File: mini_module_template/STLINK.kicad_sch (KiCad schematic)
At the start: 25 parts, among them U6 STM32F103CB, Y2 8MHz

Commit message: Leyout rev 1
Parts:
- removed Y2: 8MHz, st-link:Crystal_SMD_5032-2Pin_5.0x3.2mm, symbol Device:Crystal
- added C27: 10u, Capacitor_SMD:C_0805_2012Metric, symbol Device:C
- added C37: 100nF, Capacitor_SMD:C_0402_1005Metric, symbol Device:C
- added FB2: FerriteBead, Inductor_SMD:L_0805_2012Metric, symbol Device:FerriteBead
- added Q1: S9013, Package_TO_SOT_SMD:SOT-23, symbol Device:Q_NPN_BEC
- added R18: 10k, Resistor_SMD:R_0402_1005Metric, symbol Device:R
- added R20: 100R, Resistor_SMD:R_0402_1005Metric, symbol Device:R
- added R21: 39k, Resistor_SMD:R_0402_1005Metric, symbol Device:R
- added R22: 1K5, Resistor_SMD:R_0402_1005Metric, symbol Device:R
- added Y2: 8MHz, Crystal:Crystal_SMD_3225-4Pin_3.2x2.5mm, symbol Device:Crystal_GND24
- R17: renamed from R34; footprint Resistor_SMD:R_0402_1005Metric -> Resistor_SMD:R_0603_1608Metric
- renumbered C26 to C13, C27 to C14, C28 to C15, C29 to C16, C21 to C17, C22 to C18, C23 to C19, D9 to D4, D10 to D5, R26 to R11, R27 to R12, R35 to R13, R29 to R14, R32 to R15, R36 to R16, R37 to R19, R38 to R23, U6 to U3
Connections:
- net +3V3: now also FB2.1, Q1.3 (C); no longer C13.1, C14.1, C15.1, C16.1, U3.1 (VBAT), U3.24 (VDD), U3.36 (VDD), U3.48 (VDD), U3.9 (VDDA)
- net BOOT: now also TP2.1; no longer TP4.1
- net CLK: now also TP4.1; no longer TP3.1
- net DIO: now also TP3.1; no longer TP2.1
- net GND: now also C27.2, C37.2, R21.1, Y2.2, Y2.4
- net USB_D+: now also R22.1
- net USB_RENUM: now also R20.1
- net at C19.1, U3.6 (PD1): now also Y2.3
- net at C18.1, U3.5 (PD0): now also Y2.1
- new net: C13.1, C14.1, C15.1, C16.1, C27.1, C37.1, FB2.2, U3.1 (VBAT), U3.24 (VDD), U3.36 (VDD), U3.48 (VDD), U3.9 (VDDA)
- new net: Q1.2 (E), R22.2
- new net: Q1.1 (B), R18.1, R20.2, R21.2
- new net +5V: R18.2
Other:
- note added: "FORCE RENUMERATION OF USB DEVICES"
- note added: "SWD"
- note removed: "Decoupling"
- note removed: "Programming Pins"
- moved on the sheet: C13, C14, C15, C16

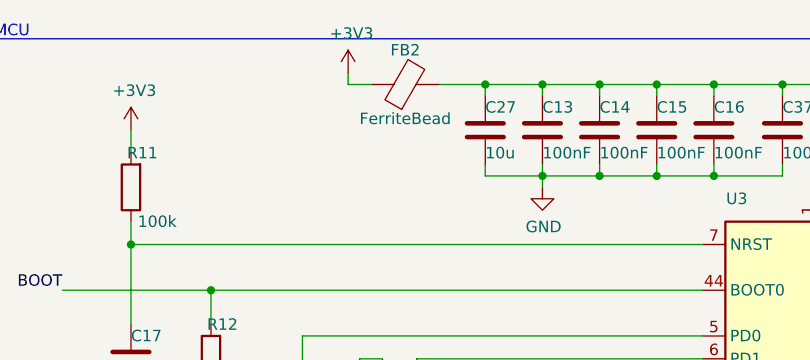
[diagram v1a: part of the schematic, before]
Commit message: fixed can and usb traces
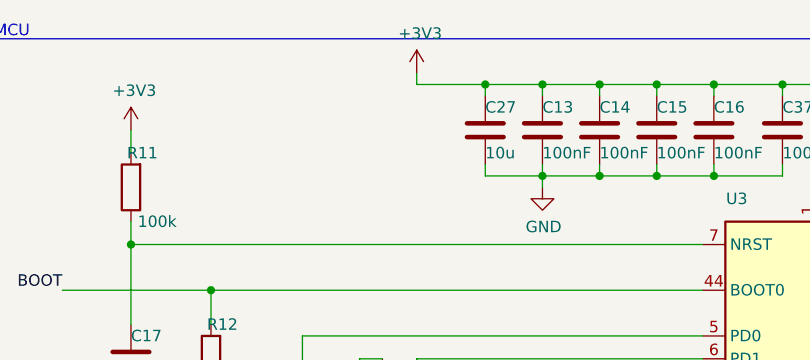
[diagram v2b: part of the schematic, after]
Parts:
- removed FB2: FerriteBead, Inductor_SMD:L_0805_2012Metric, symbol Device:FerriteBead
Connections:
- net +3V3: now also C13.1, C14.1, C15.1, C16.1, C27.1, C37.1, U3.1 (VBAT), U3.24 (VDD), U3.36 (VDD), U3.48 (VDD), U3.9 (VDDA)
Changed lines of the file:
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@@
 	(wire
 		(pts
-			(xy 67.31 20.32) (xy 72.39 20.32)
-		)
-		(stroke
-			(width 0)
-			(type default)
-		)
-	)
-	(wire
-		(pts
 			(xy 77.47 67.31) (xy 77.47 69.85)
 		)
@@
 	(wire
 		(pts
+			(xy 64.77 20.32) (xy 72.39 20.32)
+		)
+		(stroke
+			(width 0)
+			(type default)
+		)
+	)
+	(wire
+		(pts
 			(xy 260.35 49.53) (xy 260.35 52.07)
 		)
@@
 	(wire
 		(pts
-			(xy 57.15 20.32) (xy 57.15 19.05)
+			(xy 64.77 20.32) (xy 64.77 19.05)
 		)
 		(stroke
@@
 		)
 	)
-	(wire
-		(pts
-			(xy 59.69 20.32) (xy 57.15 20.32)
-		)
-		(stroke
-			(width 0)
-			(type default)
-		)
-	)
 	(rectangle
 		(start 182.88 17.78)
@@
 	)
 	(symbol
-		(lib_id "Device:FerriteBead")
-		(at 63.5 20.32 90)
-		(unit 1)
-		(exclude_from_sim no)
-		(in_bom yes)
-		(on_board yes)
-		(dnp no)
-		(property "Reference" "FB2"
-			(at 63.5 16.51 90)
-			(effects
-				(font
-					(size 1.27 1.27)
-				)
-			)
-		)
-		(property "Value" "FerriteBead"
-			(at 63.5 24.13 90)
-			(effects
-				(font
-					(size 1.27 1.27)
-				)
-			)
-		)
-		(property "Footprint" "Inductor_SMD:L_0805_2012Metric"
-			(at 63.5 22.098 90)
-			(effects
-				(font
-					(size 1.27 1.27)
-				)
-				(hide yes)
-			)
-		)
-		(property "Datasheet" "~"
-			(at 63.5 20.32 0)
-			(effects
-				(font
-					(size 1.27 1.27)
-				)
-				(hide yes)
-			)
-		)
-		(property "Description" ""
-			(at 63.5 20.32 0)
-			(effects
-				(font
-					(size 1.27 1.27)
-				)
-				(hide yes)
-			)
-		)
-		(pin "1"
-		)
-		(pin "2"
-		)
-		(instances
-			(project "mini_module_template"
-				(path "/f131027f-631c-4099-b0ec-5f883860005f/f8d1eb31-148a-4007-97b5-8e2a7921be41"
-					(reference "FB2")
-					(unit 1)
-				)
-			)
-		)
-	)
-	(symbol
 		(lib_id "Connector:TestPoint")
 		(at 262.89 45.72 270)
@@
 	(symbol
 		(lib_id "power:+3V3")
-		(at 57.15 19.05 0)
+		(at 64.77 19.05 0)
 		(unit 1)
 		(exclude_from_sim no)
@@
 		(dnp no)
 		(property "Reference" "#PWR026"
-			(at 57.15 22.86 0)
+			(at 64.77 22.86 0)
 			(effects
 				(font
@@
 		)
 		(property "Value" "+3V3"
-			(at 57.531 14.6558 0)
+			(at 65.151 14.6558 0)
 			(effects
 				(font
@@
 		)
 		(property "Footprint" ""
-			(at 57.15 19.05 0)
+			(at 64.77 19.05 0)
 			(effects
 				(font
@@
 		)
 		(property "Datasheet" ""
-			(at 57.15 19.05 0)
+			(at 64.77 19.05 0)
 			(effects
 				(font
@@
 		)
 		(property "Description" ""
-			(at 57.15 19.05 0)
+			(at 64.77 19.05 0)
 			(effects
 				(font

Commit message: updaet schematic
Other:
- company: (none) -> Patryk Dudziński
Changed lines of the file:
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@@
 	(title_block
 		(title "STLNIK v2")
+		(date "2025-01-10")
+		(rev "1.0")
+		(company "Patryk Dudziński")
 	)
 	(junction
@@
 	(label "TARGET_TX"
 		(at 134.62 71.12 0)
-		(fields_autoplaced yes)
 		(effects
 			(font
@@
 	(label "LED"
 		(at 254 111.76 180)
-		(fields_autoplaced yes)
 		(effects
 			(font
@@
 	(label "LED"
 		(at 134.62 88.9 0)
-		(fields_autoplaced yes)
 		(effects
 			(font
@@
 	(label "CLK"
 		(at 259.08 45.72 180)
-		(fields_autoplaced yes)
 		(effects
 			(font
@@
 	(label "CLK"
 		(at 134.62 101.6 0)
-		(fields_autoplaced yes)
 		(effects
 			(font
@@
 	(label "USB_RENUM"
 		(at 218.44 40.64 0)
-		(fields_autoplaced yes)
 		(effects
 			(font
@@
 	(label "DIO"
 		(at 134.62 99.06 0)
-		(fields_autoplaced yes)
 		(effects
 			(font
@@
 	(label "BOOT"
 		(at 25.4 43.18 180)
-		(fields_autoplaced yes)
 		(effects
 			(font
@@
 	(label "DIO"
 		(at 257.81 41.91 180)
-		(fields_autoplaced yes)
 		(effects
 			(font
@@
 	(label "BOOT"
 		(at 257.81 38.1 180)
-		(fields_autoplaced yes)
 		(effects
 			(font
@@
 	(label "USB_RENUM"
 		(at 134.62 104.14 0)
-		(fields_autoplaced yes)
 		(effects
 			(font
@@
 	(label "SWO"
 		(at 134.62 91.44 0)
-		(fields_autoplaced yes)
 		(effects
 			(font
@@
 	(label "TARGET_RX"
 		(at 134.62 73.66 0)
-		(fields_autoplaced yes)
 		(effects
 			(font
@@
 		(shape output)
 		(at 78.74 101.6 180)
-		(fields_autoplaced yes)
 		(effects
 			(font
@@
 		(shape input)
 		(at 134.62 96.52 0)
-		(fields_autoplaced yes)
 		(effects
 			(font
@@
 		(shape input)
 		(at 134.62 78.74 0)
-		(fields_autoplaced yes)
 		(effects
 			(font
@@
 		(shape output)
 		(at 93.98 66.04 180)
-		(fields_autoplaced yes)
 		(effects
 			(font
@@
 		(shape input)
 		(at 134.62 93.98 0)
-		(fields_autoplaced yes)
 		(effects
 			(font
@@
 		(shape output)
 		(at 78.74 99.06 180)
-		(fields_autoplaced yes)
 		(effects
 			(font
@@
 		(shape input)
 		(at 195.58 63.5 0)
-		(fields_autoplaced yes)
-		(effects
-			(font
+		(effects
+			(font
